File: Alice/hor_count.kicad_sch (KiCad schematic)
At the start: 262 parts, among them Q1 PASS, Q159 NOT_OC, Q160 NOT_OC, Q161 NOT_OC, Q162 NOT_OC, Q163 NOT_OC, Q164 NOT_OC, Q165 NOT_OC, Q166 NOT_OC, Q167 NOT_OC, Q168 NOT_OC, Q169 NOT_OC, Q170 NOT_OC, Q171 NOT_OC, Q172 NOT_OC, Q173 NOT_OC, Q174 NOT_OC, Q175 NOT_OC, Q176 NOT_OC, Q177 NOT_OC, Q178 NOT_OC, Q179 NOT_OC, Q180 NOT_OC, Q181 NOT_OC, Q182 NOT_OC, Q183 NOT_OC, Q184 NOT_OC, Q185 NOT_OC, Q186 NOT_OC, Q187 NOT_OC, Q188 NOT_OC, Q189 NOT_OC, Q190 NOT_OC, Q191 NOT_OC, Q192 NOT_OC, Q193 NOT_OC, Q194 NOT_OC, Q195 NOT_OC, Q196 NOT_OC, Q197 NOT_OC, Q198 NOT_OC, Q199 NOT_OC, Q2 PASS, Q200 NOT_OC, Q201 NOT_OC, Q202 NOT_OC, Q203 NOT_OC, Q204 NOT_OC, Q205 NOT_OC, Q206 NOT_OC, Q207 NOT_OC, Q208 NOT_OC, Q209 NOT_OC, Q210 NOT_OC, Q211 NOT_OC, Q212 NOT_OC, Q213 NOT_OC, Q214 NOT_OC, Q215 NOT_OC, Q216 NOT_OC, Q217 NOT_OC, Q218 NOT_OC, Q219 NOT_OC, Q220 NOT_OC, Q221 NOT_OC, Q222 NOT_OC, Q223 NOT_OC, Q224 NOT_OC, Q225 NOT_OC, Q226 NOT_OC, Q227 NOT_OC, Q228 NOT_OC, Q229 NOT_OC, Q230 NOT_OC, Q231 NOT_OC, Q232 NOT_OC, Q233 NOT_OC, Q234 NOT_OC, Q235 NOT_OC, Q236 NOT_OC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

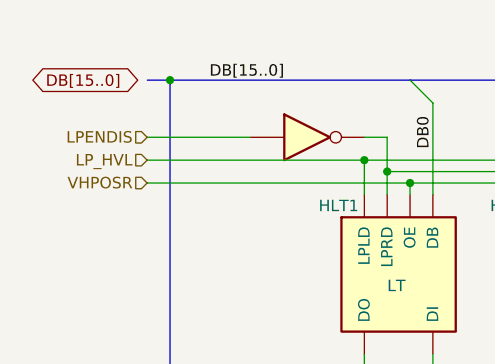
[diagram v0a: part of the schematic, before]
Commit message: Added Copper DMA schematics (WIP)
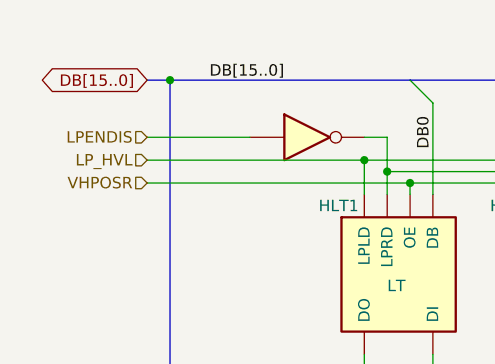
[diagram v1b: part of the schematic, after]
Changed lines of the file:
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@@
     (effects (font (size 1.27 1.27)) (justify left bottom))
   )
-  (global_label "DB[15..0]" (shape bidirectional) (at 13.97 24.13 0) (fields_autoplaced)
-    (effects (font (size 1.27 1.27)) (justify left))
-    (property "Intersheet References" "${INTERSHEET_REFS}" (id 0) (at 25.4545 24.0506 0)
-      (effects (font (size 1.27 1.27)) (justify left) hide)
+  (global_label "DB[15..0]" (shape bidirectional) (at 26.67 24.13 180) (fields_autoplaced)
+    (effects (font (size 1.27 1.27)) (justify right))
+    (property "Intersheet References" "${INTERSHEET_REFS}" (id 0) (at 15.1855 24.2094 0)
+      (effects (font (size 1.27 1.27)) (justify right) hide)
     )
   )
